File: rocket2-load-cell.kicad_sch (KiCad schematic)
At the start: 0 parts

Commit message: David's Schematic
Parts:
- added C1, C4: 10p, symbol Device:C
- added C10, C12, C13, C17, C18: 0.1uF, SparkFun_HX711_Load_Cell:0603-CAP, symbol SparkFun_HX711_Load_Cell-eagle-import:0.1UF-25V-5%(0603)
- added C11, C16: 22u, symbol Device:C
- added C14, C15: 10uF, SparkFun_HX711_Load_Cell:1210, symbol SparkFun_HX711_Load_Cell-eagle-import:10UF50V20%(1210)
- added C2: 100nF, Capacitor_SMD:C_0603_1608Metric, symbol Device:C_Small
- added C3: 10n, symbol Device:C
- added C5, C6, C7, C8, C9: 100n, symbol Device:C
- added J1: SWD, Connector_PinHeader_1.27mm:PinHeader_2x05_P1.27mm_Vertical_SMD, symbol UCIRP-KiCAD-Lib:ARM_Cortex_Debug
- added JP1: M05PTH, SparkFun_HX711_Load_Cell:1X05, symbol SparkFun_HX711_Load_Cell-eagle-import:M05PTH
- added L1: 3.3uH, SparkFun_HX711_Load_Cell:0805, symbol SparkFun_HX711_Load_Cell-eagle-import:INDUCTOR0805-IND
- added PWR_LED1: ?, symbol Device:LED
- added PWR_LED_R1: ?, symbol Device:R
- added Q1: MMBT4403, SparkFun_HX711_Load_Cell:SOT23-3, symbol SparkFun_HX711_Load_Cell-eagle-import:TRANSISTOR_PNPMMBT4403
- added R1: 20k, SparkFun_HX711_Load_Cell:0603-RES, symbol SparkFun_HX711_Load_Cell-eagle-import:20KOHM1/10W1%(0603)
- added R2: 8.2K, SparkFun_HX711_Load_Cell:0603-RES, symbol SparkFun_HX711_Load_Cell-eagle-import:8.2KOHM-1/10W-5%(0603)
- added R3, R4: 100, SparkFun_HX711_Load_Cell:0603-RES, symbol SparkFun_HX711_Load_Cell-eagle-import:100OHM-1/10W-1%(0603)
- added R5: 10K, SparkFun_HX711_Load_Cell:0603-RES, symbol SparkFun_HX711_Load_Cell-eagle-import:10KOHM-1/10W-1%(0603)0603
- added SJ1: JUMPER-PAD-2-NC_BY_TRACE, SparkFun_HX711_Load_Cell:PAD-JUMPER-2-NC_BY_TRACE_YES_SILK, symbol SparkFun_HX711_Load_Cell-eagle-import:JUMPER-PAD-2-NC_BY_TRACE
- added U1: ~, Package_SO:SOIC-8W_5.3x5.3mm_P1.27mm, symbol UCIRP-KiCAD-Lib:SST25VF016B
- added U2: STM32F103C8Tx, Package_QFP:LQFP-48_7x7mm_P0.5mm, symbol MCU_ST_STM32F1:STM32F103C8Tx
- added U3: AMS1117-3.3, Package_TO_SOT_SMD:SOT-223-3_TabPin2, symbol Regulator_Linear:AMS1117-3.3
- added U4: HX711, SparkFun_HX711_Load_Cell:SO16, symbol SparkFun_HX711_Load_Cell-eagle-import:HX711HX711
- added Y1: 16mhz, symbol Device:Crystal_GND24
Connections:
- new net: Q1.1 (B), U4.2 (BASE)
- new net: L1.2, Q1.3 (C), R1.2, U4.3 (AVDD)
- new net: R1.1, R2.2, U4.4 (VFB)
- new net: C18.2, U4.6 (VBG)
- new net: C1.1, U2.5 (PD0), Y1.1
- new net: C4.1, U2.6 (PD1), Y1.3
- new net: PWR_LED1.1 (K), PWR_LED_R1.2
- new net: R5.1, SJ1.2, U4.15 (RATE)
- new net: C17.1, R3.2, U4.7 (INA-)
- new net: C17.2, R4.2, U4.8 (INA+)
- new net +3.3V: C10.1, C12.1, C14.1, C16.1, C2.1, C3.1, C6.1, C7.1, C8.1, C9.1, J1.1 (VCC), PWR_LED1.2 (A), Q1.2 (E), R5.2, U1.8 (VDD), U2.1 (VBAT), U2.24 (VDD), U2.36 (VDD), U2.48 (VDD), U2.9 (VDDA), U3.2 (VO), U4.1 (VSUP), U4.16 (DVDD)
- new net A+: JP1.2, R4.1
- new net A-: JP1.3, R3.1
- new net AVDD: C13.1, C15.1, JP1.5, L1.1
- new net DEBUG_SWCLK: J1.4 (SWDCLK/TCK), U2.34 (PA13)
- new net DEBUG_SWDIO: J1.2 (SWDIO/TMS), U2.37 (PA14)
- new net GND: C1.2, C10.2, C11.2, C12.2, C13.2, C14.2, C15.2, C16.2, C18.1, C2.2, C3.2, C4.2, C5.1, C6.2, C7.2, C8.2, C9.2, J1.3 (GND), J1.5 (GND), J1.9 (GND_Detect), JP1.1, JP1.4, PWR_LED_R1.1, R2.1, SJ1.1, U1.4 (VSS), U2.23 (VSS), U2.35 (VSS), U2.44 (BOOT0), U2.47 (VSS), U2.8 (VSSA), U3.1 (GND), U4.10 (INB+), U4.14 (XI), U4.5 (AGND), U4.9 (INB-), Y1.2, Y1.4
- new net HX711_CLK: U2.42 (PB6), U4.11 (PD_SCK)
- new net HX711_DATA: U2.43 (PB7), U4.12 (DOUT)
- new net MEM_CS: U1.1 (~{CE}), U2.14 (PA4)
- new net MEM_HOLD: U1.7 (~{HOLD}), U2.13 (PA3)
- new net MEM_MISO: U1.2 (SO), U2.16 (PA6)
- new net MEM_MOSI: U1.5 (SI), U2.17 (PA7)
- new net MEM_SCK: U1.6 (SCK), U2.15 (PA5)
- new net MEM_WP: U1.3 (~{WP}), U2.29 (PA8)
- new net NRST: C5.2, J1.10 (~{RST}), U2.7 (NRST)
- new net VBUS: C11.1, U3.3 (VI)
- no-connect marks 0 -> 27
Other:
- note added: "A+"
- note added: "A-"
- note added: "AVDD = VBG(R1+R2)/R2"
- note added: "Default: Closed - Data rate set to 10SPS"
- note added: "E+"
- note added: "E-"
- note added: "IO: 2.7-5.5V"
- note added: "Open jumper to set to 80SPS Increases noise per read"
- note added: "Shield"
- note added: "VBG = 1.25V"
- note added: "VCC: 2.7-5.5V"
- note added: "VDD: 2.7-5.5V"

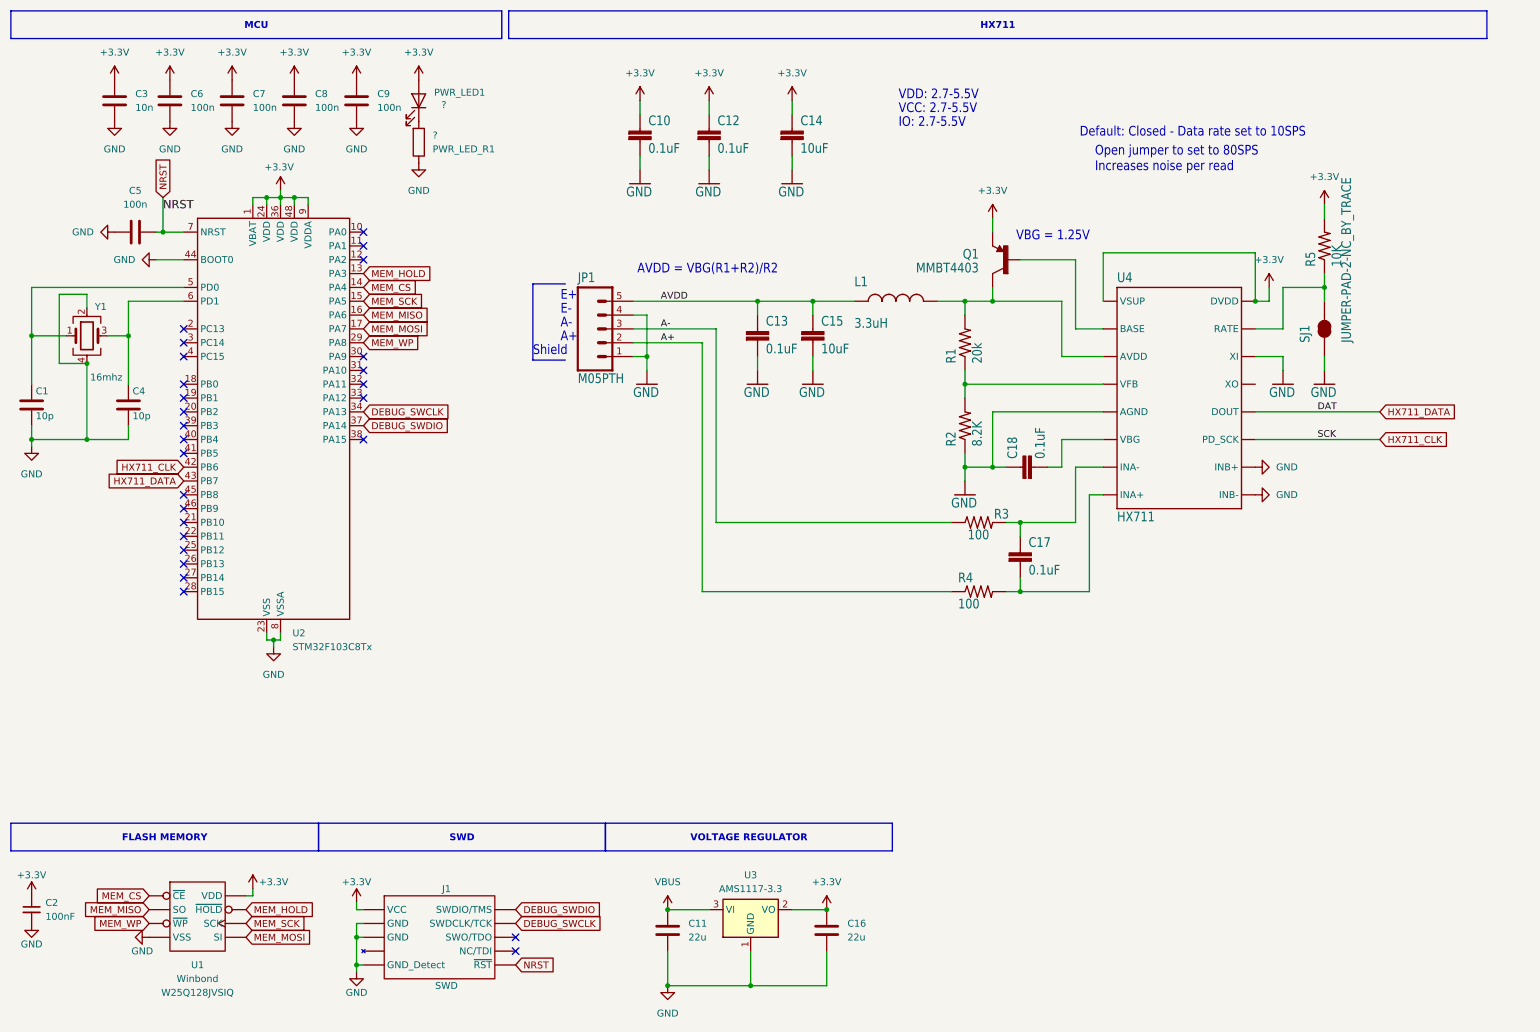
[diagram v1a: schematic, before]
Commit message: HSE Crystal (16MHz) and Adjusted AVDD (10.625V)
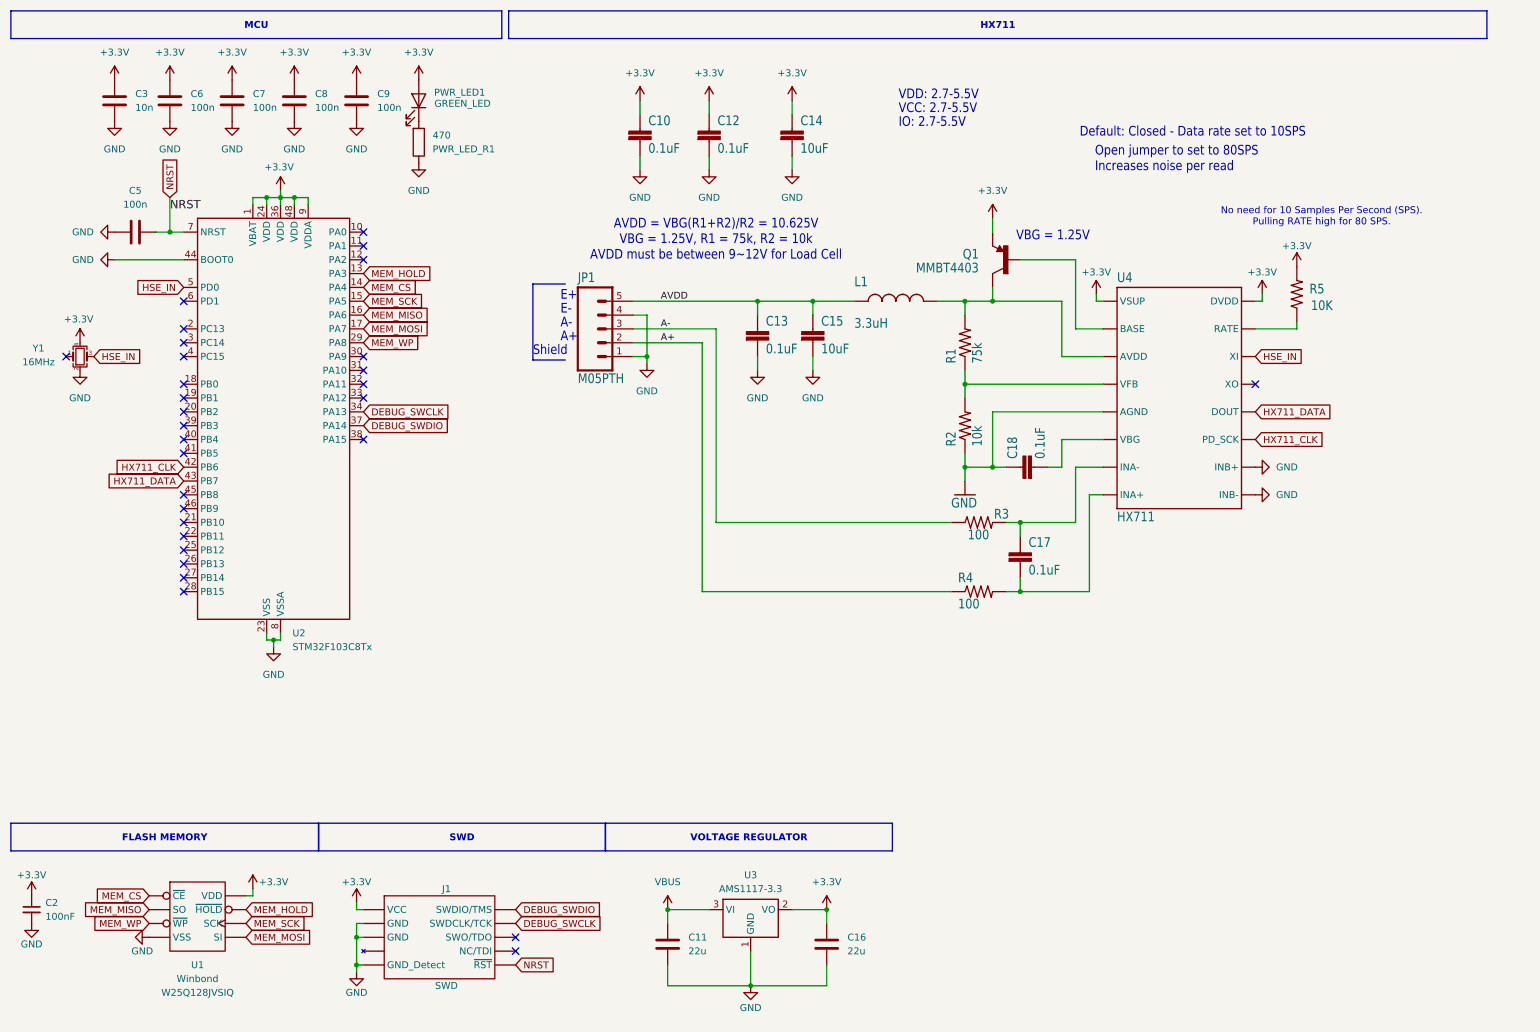
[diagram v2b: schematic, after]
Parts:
- removed C1, C4: 10p, symbol Device:C
- removed SJ1: JUMPER-PAD-2-NC_BY_TRACE, SparkFun_HX711_Load_Cell:PAD-JUMPER-2-NC_BY_TRACE_YES_SILK, symbol SparkFun_HX711_Load_Cell-eagle-import:JUMPER-PAD-2-NC_BY_TRACE
- removed Y1: 16mhz, symbol Device:Crystal_GND24
- added Y1: 16MHz, Crystal:Crystal_SMD_2520-4Pin_2.5x2.0mm, symbol Device:Crystal_GND24_Small
- PWR_LED1: value ? -> GREEN_LED
- PWR_LED_R1: value ? -> 470
- R1: value 20k -> 75k
- R2: value 8.2K -> 10k
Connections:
- net +3.3V: now also Y1.4
- net GND: now also Y1.2; no longer U4.14 (XI)
- net HSE_IN: now reaches U2.5 (PD0)
- net HSE_IN: now also U4.14 (XI), Y1.3
- no-connect marks 27 -> 30
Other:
- note added: "AVDD = VBG(R1+R2)/R2 = 10.625V VBG = 1.25V, R1 = 75k, R2 = 10k AVDD must be between 9~12V for Load Cell"
- note added: "No need for 10 Samples Per Second (SPS). Pulling RATE high for 80 SPS."
- note removed: "AVDD = VBG(R1+R2)/R2"
- moved on the sheet: C11, C16, R5

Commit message: Changed to small components. Added +5V power supply
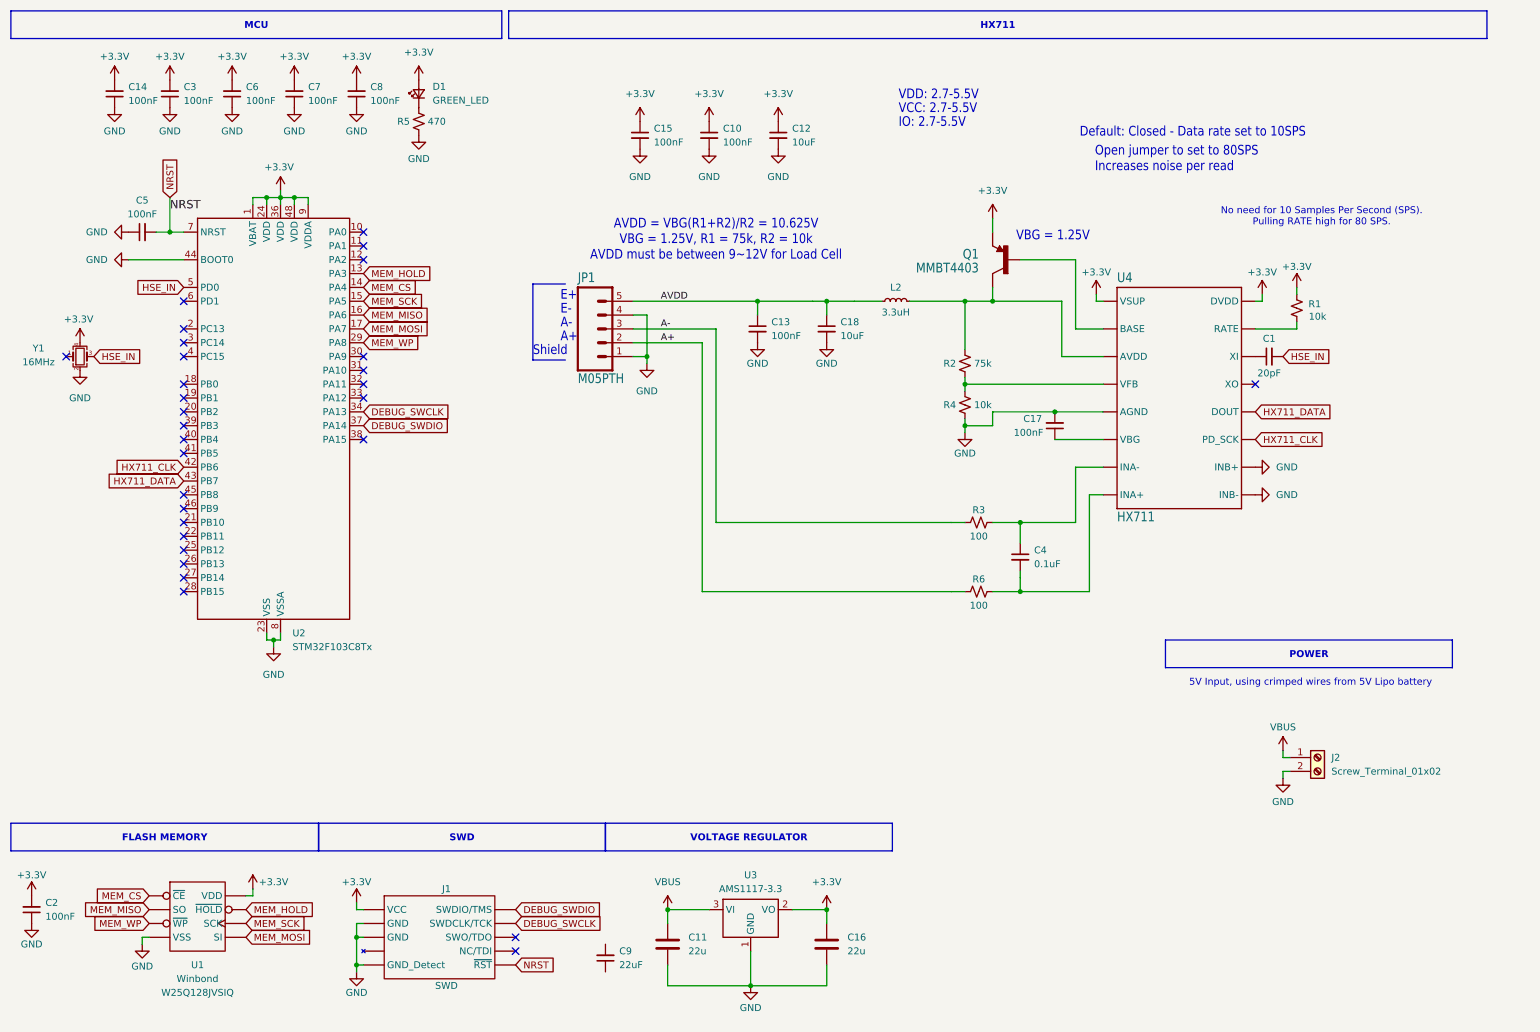
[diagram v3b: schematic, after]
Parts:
- removed C10, C12, C13, C17, C18: 0.1uF, SparkFun_HX711_Load_Cell:0603-CAP, symbol SparkFun_HX711_Load_Cell-eagle-import:0.1UF-25V-5%(0603)
- removed C14, C15: 10uF, SparkFun_HX711_Load_Cell:1210, symbol SparkFun_HX711_Load_Cell-eagle-import:10UF50V20%(1210)
- removed C3: 10n, symbol Device:C
- removed C5, C6, C7, C8, C9: 100n, symbol Device:C
- removed L1: 3.3uH, SparkFun_HX711_Load_Cell:0805, symbol SparkFun_HX711_Load_Cell-eagle-import:INDUCTOR0805-IND
- removed PWR_LED1: GREEN_LED, symbol Device:LED
- removed PWR_LED_R1: 470, symbol Device:R
- removed R1: 75k, SparkFun_HX711_Load_Cell:0603-RES, symbol SparkFun_HX711_Load_Cell-eagle-import:20KOHM1/10W1%(0603)
- removed R2: 10k, SparkFun_HX711_Load_Cell:0603-RES, symbol SparkFun_HX711_Load_Cell-eagle-import:8.2KOHM-1/10W-5%(0603)
- removed R3, R4: 100, SparkFun_HX711_Load_Cell:0603-RES, symbol SparkFun_HX711_Load_Cell-eagle-import:100OHM-1/10W-1%(0603)
- removed R5: 10K, SparkFun_HX711_Load_Cell:0603-RES, symbol SparkFun_HX711_Load_Cell-eagle-import:10KOHM-1/10W-1%(0603)0603
- added C1: 20pF, symbol Device:C_Small
- added C10, C13, C14, C15, C17, C3, C5, C6, C7, C8: 100nF, symbol Device:C_Small
- added C12, C18: 10uF, symbol Device:C_Small
- added C4: 0.1uF, symbol Device:C_Small
- added C9: 22uF, symbol Device:C_Small
- added D1: GREEN_LED, symbol Device:LED_Small
- added J2: Screw_Terminal_01x02, symbol Connector:Screw_Terminal_01x02
- added L2: 3.3uH, symbol Device:L_Small
- added R1, R4: 10k, symbol Device:R_Small_US
- added R2: 75k, symbol Device:R_Small_US
- added R3, R6: 100, symbol Device:R_Small_US
- added R5: 470, symbol Device:R_Small_US
- C2: footprint Capacitor_SMD:C_0603_1608Metric -> (none); Manufacturer Generic -> (none); Part # Generic 0603 6.3V 100nF X7R MLCC -> (none)
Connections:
- net +3.3V: now also C2.2, C10.1, C12.1, C14.2, C15.1, C3.2, C6.2, C7.2, C8.2, D1.2 (A), R1.2; no longer C2.1
- net A+: now also R6.1
- net A-: now also R3.1
- net AVDD: now also C13.1, C18.1, L2.1
- net GND: now also C2.1, C10.2, C12.2, C13.2, C14.1, C15.2, C17.2, C18.2, C3.1, C5.1, C6.1, C7.1, C8.1, J2.2 (Pin_2), R4.1, R5.1; no longer C2.2
- net HSE_IN: now also C1.2; no longer U4.14 (XI)
- net NRST: now also C5.2
- net VBUS: now also J2.1 (Pin_1)
- net at Q1.3 (C), U4.3 (AVDD): now also L2.2, R2.2
- net at U4.4 (VFB): now also R2.1, R4.2
- net at U4.6 (VBG): now also C17.1
- net at U4.15 (RATE): now also R1.1
- net at U4.7 (INA-): now also C4.1, R3.2
- net at U4.8 (INA+): now also C4.2, R6.2
- new net: C1.1, U4.14 (XI)
- new net: D1.1 (K), R5.2
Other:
- note added: "5V Input, using crimped wires from 5V Lipo battery"

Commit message: Tidied up schematic, added comments for Daniel
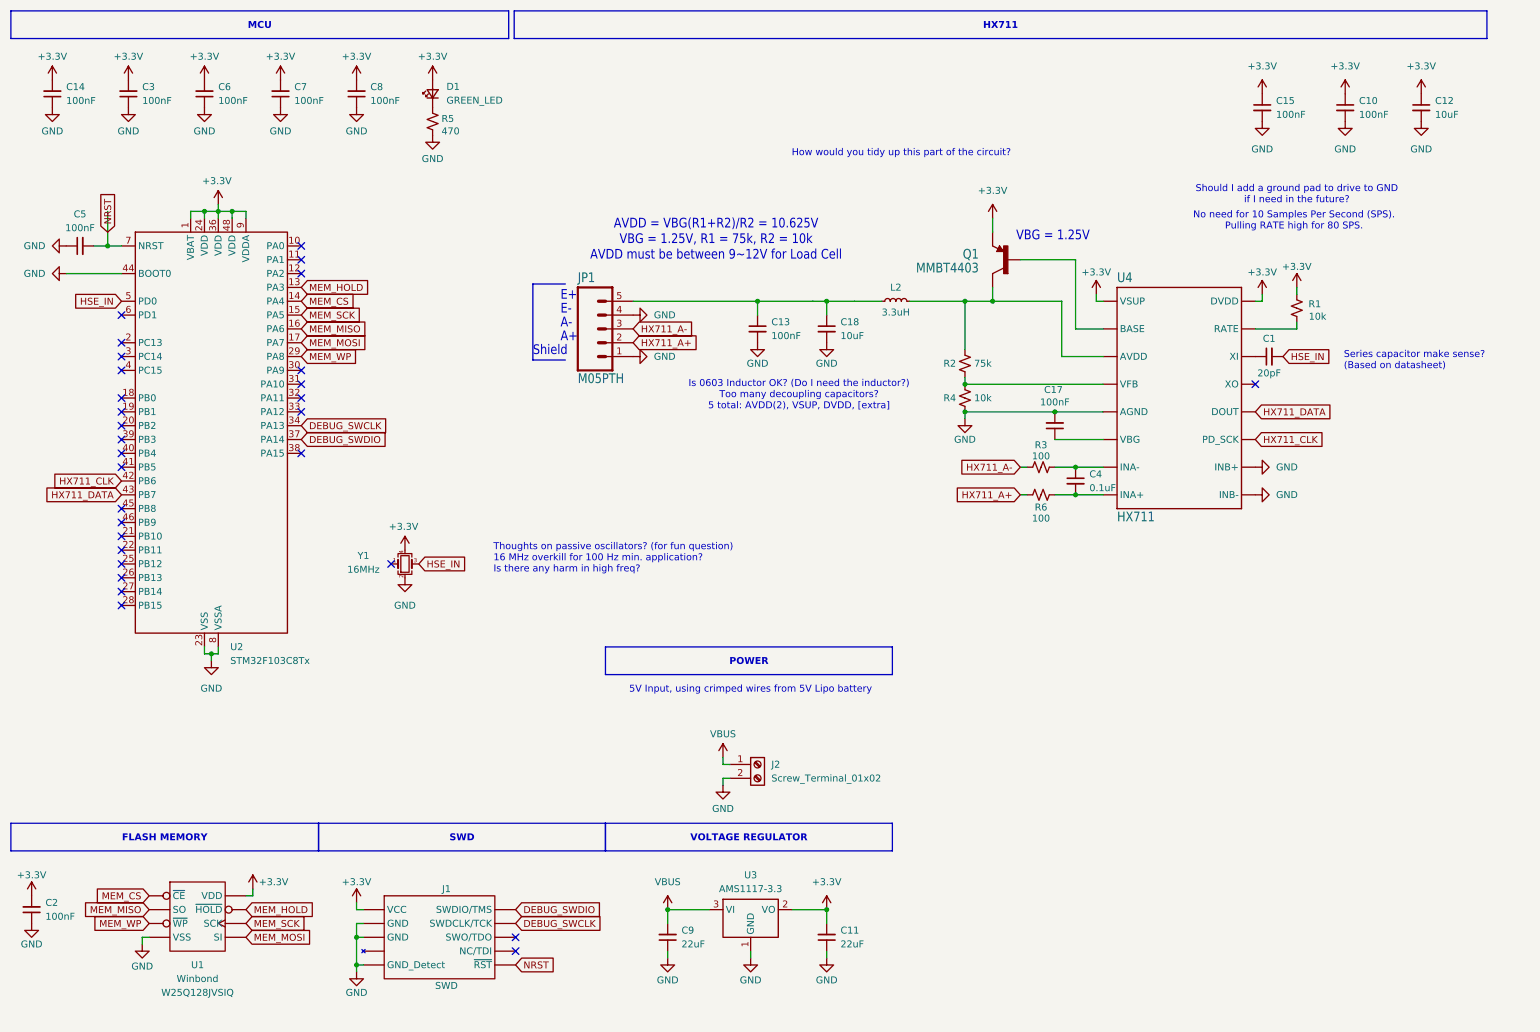
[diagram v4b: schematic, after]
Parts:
- removed C11, C16: 22u, symbol Device:C
- added C11: 22uF, Capacitor_SMD:C_0603_1608Metric, symbol Device:C_Small
- C1, C10, C12, C13, C14, C15, C17, C18, C2, C3, C4, C5, C6, C7, C8, C9: footprint (none) -> Capacitor_SMD:C_0603_1608Metric
- D1: footprint (none) -> LED_SMD:LED_0603_1608Metric
- J2: footprint (none) -> TerminalBlock_Phoenix:TerminalBlock_Phoenix_MKDS-1,5-2-5.08_1x02_P5.08mm_Horizontal
- JP1: footprint SparkFun_HX711_Load_Cell:1X05 -> TerminalBlock_Phoenix:TerminalBlock_Phoenix_MKDS-1,5-5-5.08_1x05_P5.08mm_Horizontal
- L2: footprint (none) -> Inductor_SMD:L_0603_1608Metric
- Q1: footprint SparkFun_HX711_Load_Cell:SOT23-3 -> (none)
- R1, R2, R3, R4, R5, R6: footprint (none) -> Resistor_SMD:R_0603_1608Metric
- U4: footprint SparkFun_HX711_Load_Cell:SO16 -> Package_SO:SOP-16_3.9x9.9mm_P1.27mm
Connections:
- net +3.3V: now also C11.2
- net GND: now also C9.1, C11.1
- net VBUS: now also C9.2
- net A+ renamed HX711_A+
- net A- renamed HX711_A-
- net AVDD: no longer names the net of C13.1, C18.1, JP1.5, L2.1
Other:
- note added: "How would you tidy up this part of the circuit?"
- note added: "Is 0603 Inductor OK? (Do I need the inductor?) Too many decoupling capacitors? 5 total: AVDD(2), VSUP, DVDD, [extra]"
- note added: "Series capacitor make sense? (Based on datasheet)"
- note added: "Should I add a ground pad to drive to GND if I need in the future?"
- note added: "Thoughts on passive oscillators? (for fun question) 16 MHz overkill for 100 Hz min. application? Is there any harm in high freq?"
- note removed: "Default: Closed - Data rate set to 10SPS"
- note removed: "IO: 2.7-5.5V"
- note removed: "Open jumper to set to 80SPS Increases noise per read"
- note removed: "VCC: 2.7-5.5V"
- note removed: "VDD: 2.7-5.5V"
- moved on the sheet: C10, C12, C14, C15, C3, C4, C5, C6, C7, C9, D1, R3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
